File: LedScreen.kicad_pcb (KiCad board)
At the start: 2 copper layers, 75 x 75 mm, 42 parts

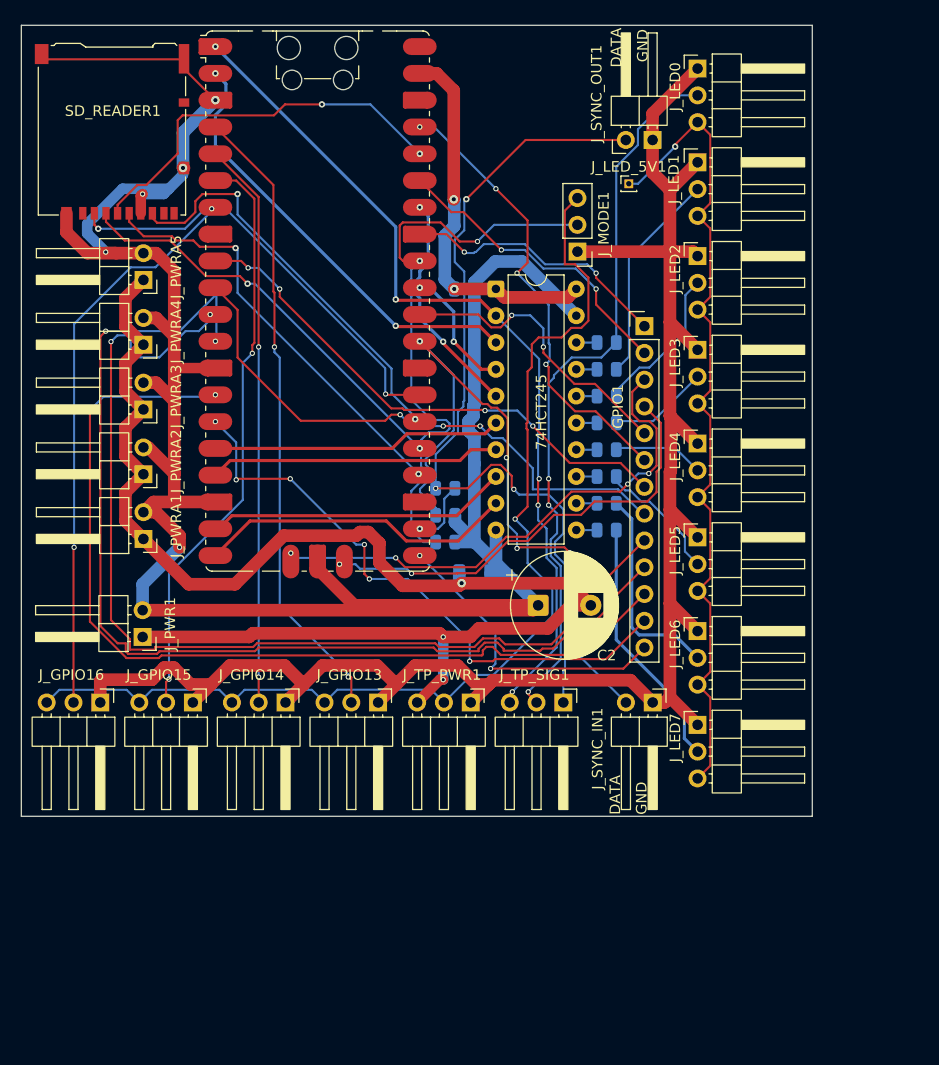
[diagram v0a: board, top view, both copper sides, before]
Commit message: removed all tracks
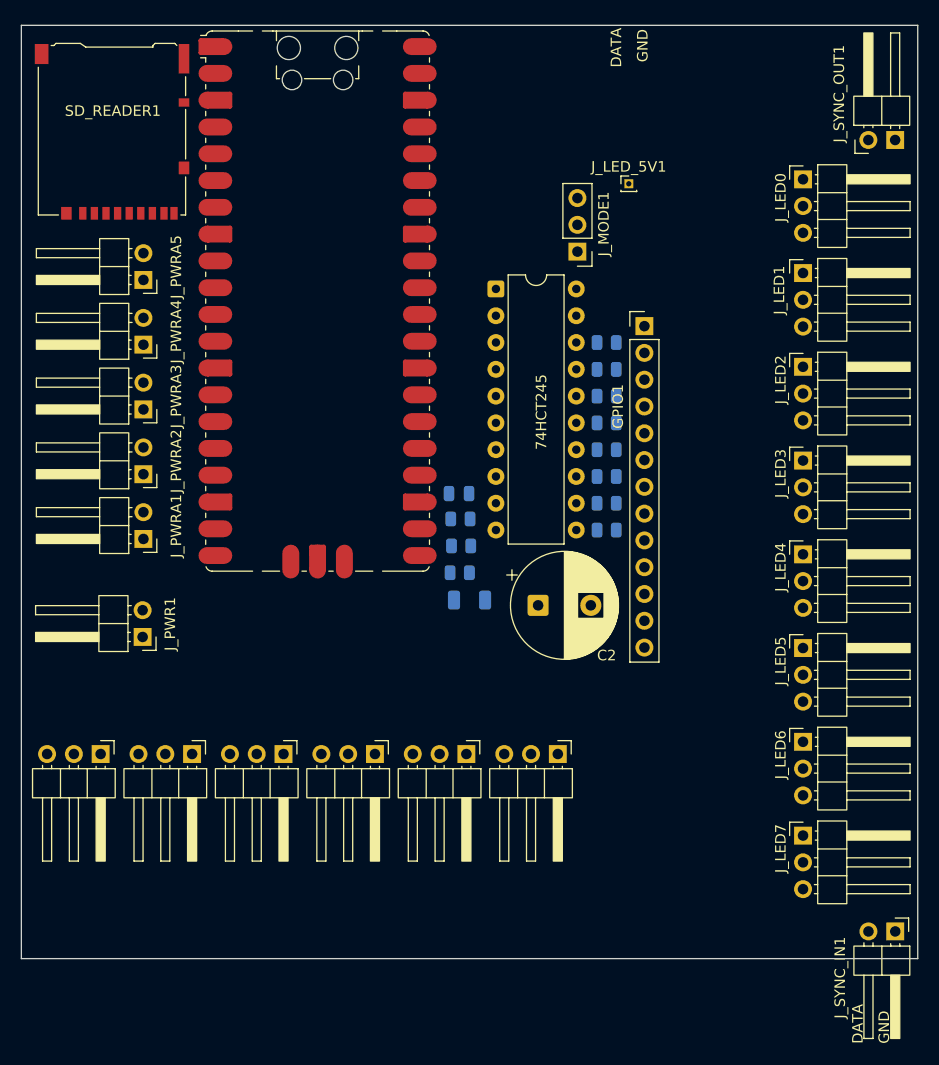
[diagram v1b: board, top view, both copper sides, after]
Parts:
- moved J_TP_SIG1 44.1 mm to (7.52, 69.1)
- moved J_SYNC_IN1 31.6 mm to (82.9, 85.9)
- moved J_TP_PWR1 26.9 mm to (16.2, 69.1)
- moved J_SYNC_OUT1 23.0 mm to (80.3, 10.9)
- moved C1 19.4 mm to (41.5, 44.4)
- moved J_GPIO16 18.1 mm to (24.9, 69.1)
- moved J_GPIO15 17.9 mm to (33.5, 69.1)
- moved J_GPIO14 17.8 mm to (42.2, 69.1)
- moved J_GPIO13 17.7 mm to (50.9, 69.1)
- moved J_LED0 14.5 mm to (74.1, 14.6)
- moved J_LED1 14.5 mm to (74.1, 23.5)
- moved J_LED2 14.5 mm to (74.1, 32.4)
- moved J_LED3 14.5 mm to (74.1, 41.3)
- moved J_LED4 14.5 mm to (74.1, 50.2)
- moved J_LED7 14.5 mm to (74.1, 76.8)
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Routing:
- net GND: track 404.5 -> 0.00 mm, vias 5 -> 0
- net +5V: track 169.0 -> 0.00 mm, vias 5 -> 0
- net +3V3: track 140.4 -> 0.00 mm, vias 3 -> 0
- net GPIO9: track 103.0 -> 0.00 mm, vias 2 -> 0
- net GPIO8: track 99.4 -> 0.00 mm, vias 2 -> 0
- net GPIO10: track 89.9 -> 0.00 mm, vias 2 -> 0
- net T_OUT0: track 82.3 -> 0.00 mm, vias 5 -> 0
- net SYNC_OUT: track 82.0 -> 0.00 mm, vias 3 -> 0
- net LED_PIN3: track 78.3 -> 0.00 mm, vias 1 -> 0
- net LED0_DATA: track 69.1 -> 0.00 mm, vias 3 -> 0
- net SYNC_IN: track 66.1 -> 0.00 mm, vias 4 -> 0
- net GPIO2: track 60.1 -> 0.00 mm, vias 2 -> 0
- net MODE: track 58.0 -> 0.00 mm, vias 2 -> 0
- net GPIO11: track 56.6 -> 0.00 mm, vias 6 -> 0
- net GPIO4: track 55.6 -> 0.00 mm, vias 2 -> 0
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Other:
- board size 75 x 75 mm -> 85 x 88.5 mm

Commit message: finsighed new v2 routing
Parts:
- removed J_LED_5V1: Conn_01x01_Pin, Connector_PinHeader_1.00mm:PinHeader_1x01_P1.00mm_Vertical
- removed J_PWRA2, J_PWRA3, J_PWRA4, J_PWRA5: Conn_01x02, Connector_PinHeader_2.54mm:PinHeader_1x02_P2.54mm_Horizontal
- added V5: Conn_01x01_Pin, Connector_PinHeader_2.54mm:PinHeader_1x01_P2.54mm_Vertical, F.Cu at (88.9, 134.4)
- A1: footprint Module:RaspberryPi_Pico_SMD_HandSolder -> Module:RaspberryPi_Pico_Common_THT
- C1, C3, R_MODE_PD1, R_SYNC_PD1, R_SYNC_SER1: moved to F.Cu
- J_GPIO13, J_GPIO14, J_GPIO15, J_GPIO16, J_LED0, J_LED1, J_LED2, J_LED3, J_LED4, J_LED5, J_LED6, J_LED7: footprint Connector_PinHeader_2.54mm:PinHeader_1x03_P2.54mm_Horizontal -> Connector_JST:JST_XH_S3B-XH-SM4-TB_1x03-1MP_P2.50mm_Horizontal
- J_PWR1: value Conn_01x02 -> Conn_01x03; footprint Connector_PinHeader_2.54mm:PinHeader_1x02_P2.54mm_Horizontal -> Connector_JST:JST_XH_S3B-XH-SM4-TB_1x03-1MP_P2.50mm_Horizontal
- J_PWRA1: value Conn_01x02 -> Conn_01x10; footprint Connector_PinHeader_2.54mm:PinHeader_1x02_P2.54mm_Horizontal -> Connector_PinHeader_2.54mm:PinHeader_1x10_P2.54mm_Vertical
- J_TP_PWR1, J_TP_SIG1: footprint Connector_PinHeader_2.54mm:PinHeader_1x03_P2.54mm_Horizontal -> Connector_PinHeader_2.54mm:PinHeader_1x03_P2.54mm_Vertical
- R1, R2, R3, R4, R5, R6, R7, R8: value 330 (0-330) -> 0R; footprint Resistor_SMD:R_0805_2012Metric -> Resistor_SMD:R_1206_3216Metric; moved to F.Cu
- moved J_LED2 141.0 mm to (166.8, 138.6)
- moved J_LED1 137.3 mm to (167.7, 124.0), turned to 90 degrees
- moved R1 136.7 mm to (155.8, 122.9), turned to -90 degrees
- moved J_LED0 133.0 mm to (167.7, 109.1), turned to 90 degrees
- moved R2 132.5 mm to (152.5, 122.9), turned to -90 degrees
- moved R3 128.3 mm to (149.2, 122.9), turned to -90 degrees
- moved J_GPIO14 125.9 mm to (167.7, 79.2), turned to 90 degrees
- moved J_LED3 124.9 mm to (152.3, 138.6)
- moved R4 124.2 mm to (145.9, 122.9), turned to -90 degrees
- moved C1 122.3 mm to (155.6, 88.5), turned to -90 degrees
- moved SD_READER1 120.7 mm to (113.3, 70.2)
- moved R5 120.0 mm to (142.6, 122.9), turned to -90 degrees
- moved J_SYNC_OUT1 119.9 mm to (163.3, 97.3), turned to 0 degrees
- moved 74HCT245 117.8 mm to (144.9, 87.4)
- moved R6 115.9 mm to (139.3, 122.9), turned to -90 degrees
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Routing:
- net +3V3: track 0.00 -> 147.7 mm, vias 0 -> 6
- net LED_PIN3: track 0.00 -> 137.0 mm
- net GPIO3: track 0.00 -> 127.3 mm, vias 0 -> 2
- net +5V: track 0.00 -> 122.2 mm
- net SYNC_OUT: track 0.00 -> 92.8 mm, vias 0 -> 2
- net GPIO2: track 0.00 -> 90.6 mm, vias 0 -> 2
- net T_OUT0: track 0.00 -> 86.6 mm, vias 0 -> 6
- net LED0_DATA: track 0.00 -> 83.2 mm
- net MODE: track 0.00 -> 72.6 mm, vias 0 -> 5
- net GPIO4: track 0.00 -> 71.5 mm, vias 0 -> 2
- net SYNC_OUT_DRV: track 0.00 -> 66.9 mm, vias 0 -> 2
- net T_OUT1: track 0.00 -> 66.3 mm, vias 0 -> 4
- net GPIO5: track 0.00 -> 64.3 mm, vias 0 -> 2
- net SYNC_IN: track 0.00 -> 49.9 mm, vias 0 -> 3
- net T_OUT3: track 0.00 -> 49.1 mm, vias 0 -> 3
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- added copper zone on B.Cu, net GND
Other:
- board size 85 x 88.5 mm -> 87 x 84 mm
- board text removed: "DATA"
- board text removed: "GND"
